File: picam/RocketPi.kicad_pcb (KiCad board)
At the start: 4 copper layers, 65 x 30 mm, 39 parts, among them J1 CAN Communication, J2 Connector_Conn_01x05_Female, J3 Conn_02x20_Counter_Clockwise_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, M1 MountingHole_2.7mm, M2 MountingHole_2.7mm, M3 MountingHole_2.7mm, M4 MountingHole_2.7mm, Q1 BSS138, Q2 AOD417, Q3 BSS138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

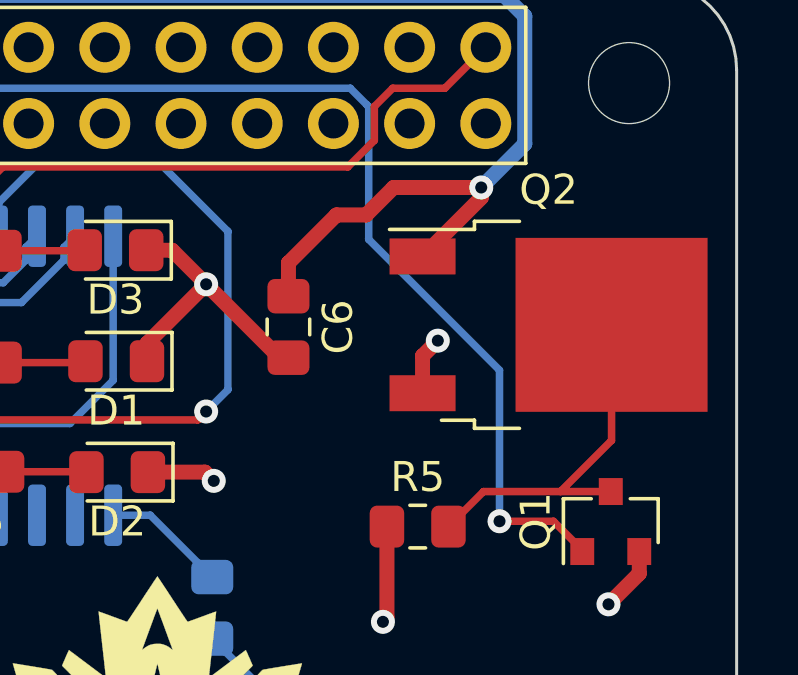
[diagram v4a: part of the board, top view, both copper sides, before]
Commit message: Fix AOD417 wiring
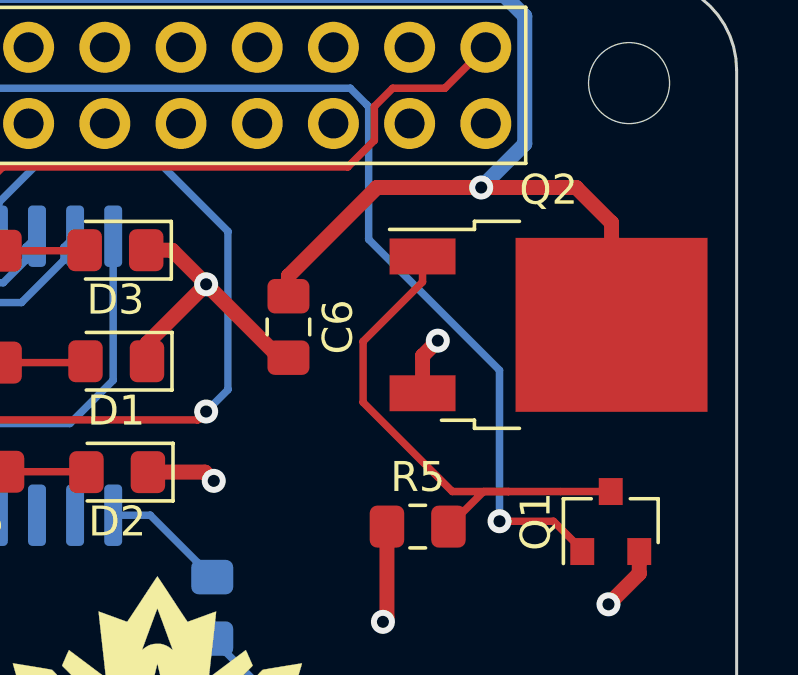
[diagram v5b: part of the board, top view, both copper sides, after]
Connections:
- Q2 pad 1: /power_pi -> Net-(Q1-Pad3)
- Q2 pad 2: Net-(Q1-Pad3) -> /power_pi
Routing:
- net Net-(Q1-Pad3): track 12.2 -> 17.7 mm
- net /power_pi: track 71.0 -> 76.2 mm
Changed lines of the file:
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@@
     (thickness 1.6)
     (drawings 21)
-    (tracks 363)
+    (tracks 368)
     (zones 0)
     (modules 39)
@@
     (pad "" smd rect (at 3.775 1.525) (size 3.05 2.75) (layers F.Paste))
     (pad 2 smd rect (at 2.1 0) (size 6.4 5.8) (layers F.Cu F.Mask)
-      (net 45 "Net-(Q1-Pad3)"))
+      (net 7 /power_pi))
     (pad 3 smd rect (at -4.2 2.28) (size 2.2 1.2) (layers F.Cu F.Paste F.Mask)
       (net 3 +5V))
     (pad 1 smd rect (at -4.2 -2.28) (size 2.2 1.2) (layers F.Cu F.Paste F.Mask)
-      (net 7 /power_pi))
+      (net 45 "Net-(Q1-Pad3)"))
     (model ${KISYS3DMOD}/Package_TO_SOT_SMD.3dshapes/TO-252-2.wrl
       (at (xyz 0 0 0))
@@
   (segment (start 74.281399 43.574601) (end 74.281399 43.549201) (width 0.5) (layer B.Cu) (net 7))
   (via (at 121.539 49.0982) (size 0.8) (drill 0.4) (layers F.Cu B.Cu) (net 7))
-  (segment (start 121.539 49.0982) (end 121.539 49.4404) (width 0.5) (layer F.Cu) (net 7))
-  (segment (start 121.539 49.4404) (end 119.5832 51.3962) (width 0.5) (layer F.Cu) (net 7))
   (segment (start 74.306799 43.574601) (end 75.184 42.6974) (width 0.5) (layer B.Cu) (net 7))
   (segment (start 74.281399 43.574601) (end 74.306799 43.574601) (width 0.5) (layer B.Cu) (net 7))
@@
   (segment (start 77.6986 42.6974) (end 122.301 42.6974) (width 0.5) (layer B.Cu) (net 7))
   (segment (start 122.301 42.6974) (end 122.991401 43.387801) (width 0.5) (layer B.Cu) (net 7))
-  (segment (start 118.618 49.0982) (end 121.539 49.0982) (width 0.5) (layer F.Cu) (net 7))
-  (segment (start 117.7036 50.0126) (end 118.618 49.0982) (width 0.5) (layer F.Cu) (net 7))
-  (segment (start 117.7036 50.0126) (end 116.713 50.0126) (width 0.5) (layer F.Cu) (net 7))
-  (segment (start 115.1128 51.6128) (end 115.1128 52.7214) (width 0.5) (layer F.Cu) (net 7))
-  (segment (start 116.713 50.0126) (end 115.1128 51.6128) (width 0.5) (layer F.Cu) (net 7))
+  (segment (start 125.8832 53.6762) (end 125.5832 53.6762) (width 0.5) (layer F.Cu) (net 7))
+  (segment (start 125.8832 50.2762) (end 125.8832 53.6762) (width 0.5) (layer F.Cu) (net 7))
+  (segment (start 124.7052 49.0982) (end 125.8832 50.2762) (width 0.5) (layer F.Cu) (net 7))
+  (segment (start 121.539 49.0982) (end 124.7052 49.0982) (width 0.5) (layer F.Cu) (net 7))
+  (segment (start 120.973315 49.0982) (end 121.539 49.0982) (width 0.5) (layer F.Cu) (net 7))
+  (segment (start 118.061 49.0982) (end 120.973315 49.0982) (width 0.5) (layer F.Cu) (net 7))
+  (segment (start 115.1128 52.0464) (end 118.061 49.0982) (width 0.5) (layer F.Cu) (net 7))
+  (segment (start 115.1128 52.7214) (end 115.1128 52.0464) (width 0.5) (layer F.Cu) (net 7))
   (segment (start 73.4314 52.4166) (end 73.406 52.442) (width 0.25) (layer F.Cu) (net 8))
   (segment (start 79.3142 50.7298) (end 79.2948 50.7492) (width 0.25) (layer F.Cu) (net 8))
@@
   (segment (start 120.4468 60.4012) (end 121.6152 59.2328) (width 0.25) (layer F.Cu) (net 45))
   (segment (start 124.1806 59.2328) (end 125.857 59.2328) (width 0.25) (layer F.Cu) (net 45))
-  (segment (start 121.6152 59.2328) (end 124.1806 59.2328) (width 0.25) (layer F.Cu) (net 45))
-  (segment (start 125.8832 57.5302) (end 125.8832 53.6762) (width 0.25) (layer F.Cu) (net 45))
-  (segment (start 124.1806 59.2328) (end 125.8832 57.5302) (width 0.25) (layer F.Cu) (net 45))
+  (segment (start 119.5832 52.2462) (end 117.602 54.2274) (width 0.25) (layer F.Cu) (net 45))
+  (segment (start 119.5832 51.3962) (end 119.5832 52.2462) (width 0.25) (layer F.Cu) (net 45))
+  (segment (start 120.574798 59.2328) (end 122.4534 59.2328) (width 0.25) (layer F.Cu) (net 45))
+  (segment (start 117.602 56.260002) (end 120.574798 59.2328) (width 0.25) (layer F.Cu) (net 45))
+  (segment (start 117.602 54.2274) (end 117.602 56.260002) (width 0.25) (layer F.Cu) (net 45))
+  (segment (start 121.6152 59.2328) (end 122.4534 59.2328) (width 0.25) (layer F.Cu) (net 45))
+  (segment (start 122.4534 59.2328) (end 124.1806 59.2328) (width 0.25) (layer F.Cu) (net 45))
   (segment (start 94.916431 48.139601) (end 99.612199 48.139601) (width 0.25) (layer B.Cu) (net 46))
   (segment (start 93.13151 49.924522) (end 94.916431 48.139601) (width 0.25) (layer B.Cu) (net 46))

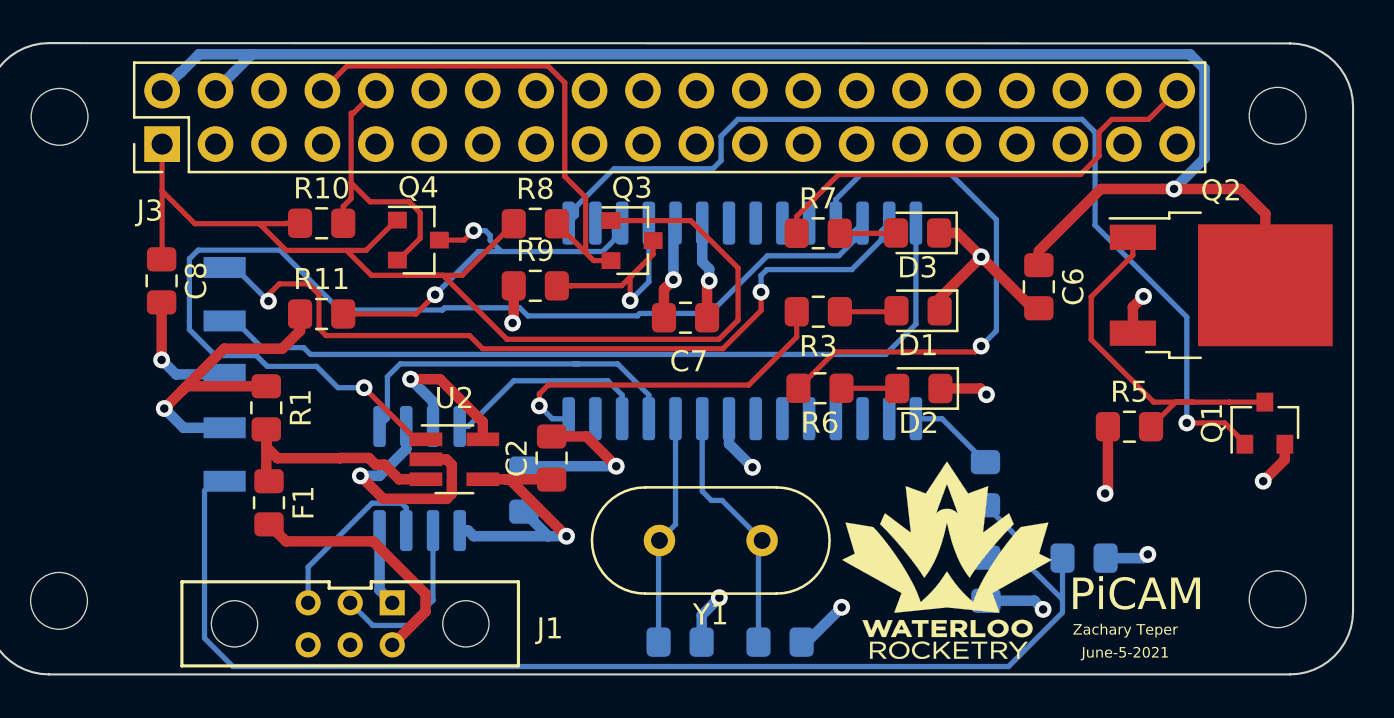
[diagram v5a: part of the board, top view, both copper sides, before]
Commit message: Rotate CAN connector 180 degrees
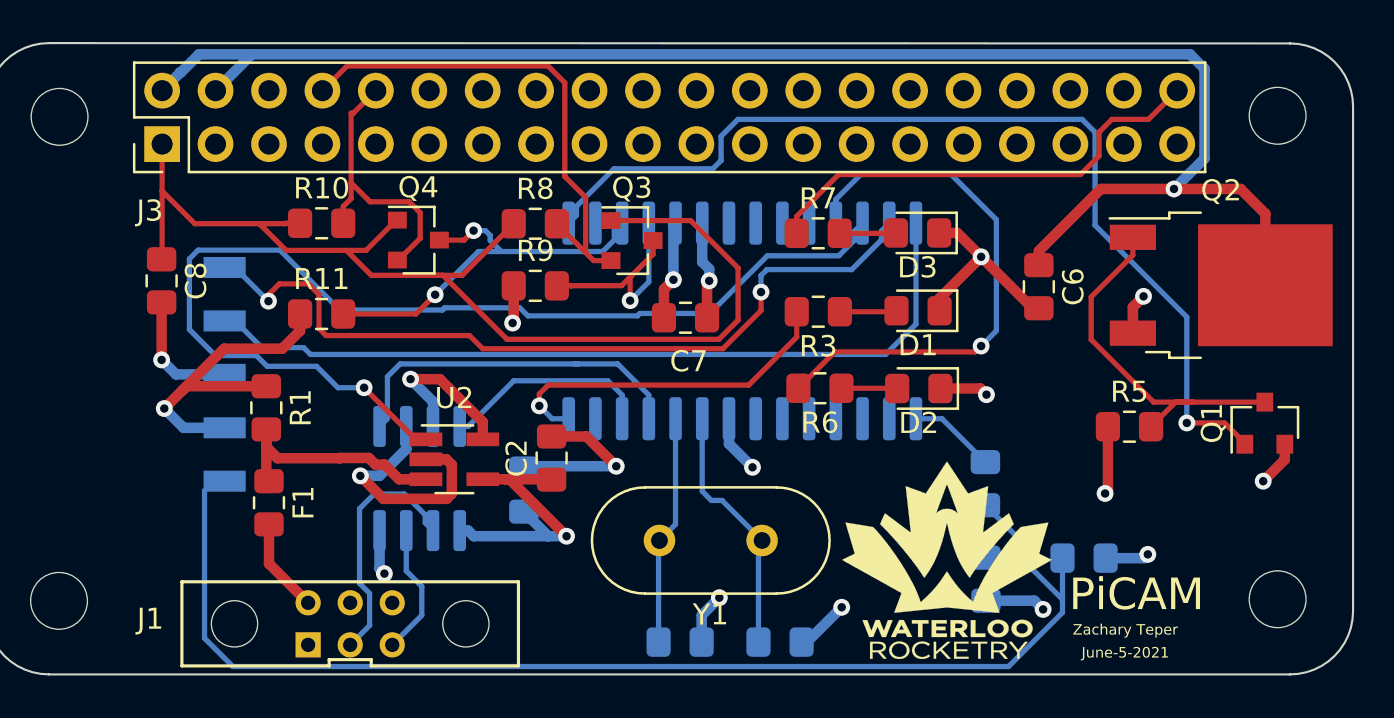
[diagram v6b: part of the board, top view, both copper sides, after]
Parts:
- turned J1 to 0 degrees
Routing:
- net Net-(F1-Pad2): track 11.9 -> 4.50 mm
- net /CANL: track 8.19 -> 11.8 mm
- net /CANH: track 8.79 -> 6.32 mm
- net GND: track 57.9 -> 56.4 mm, vias 11 -> 12

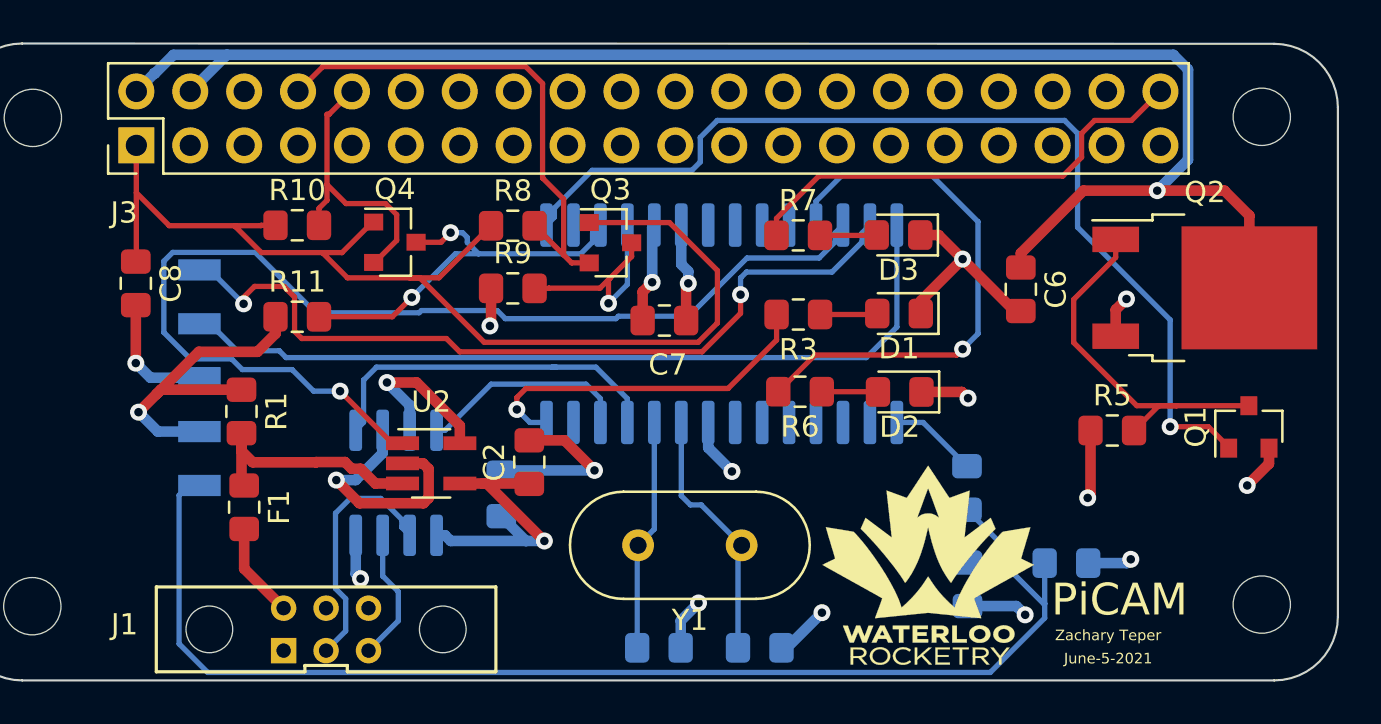
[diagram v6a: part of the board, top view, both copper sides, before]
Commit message: Add gate resistor and redo some routing
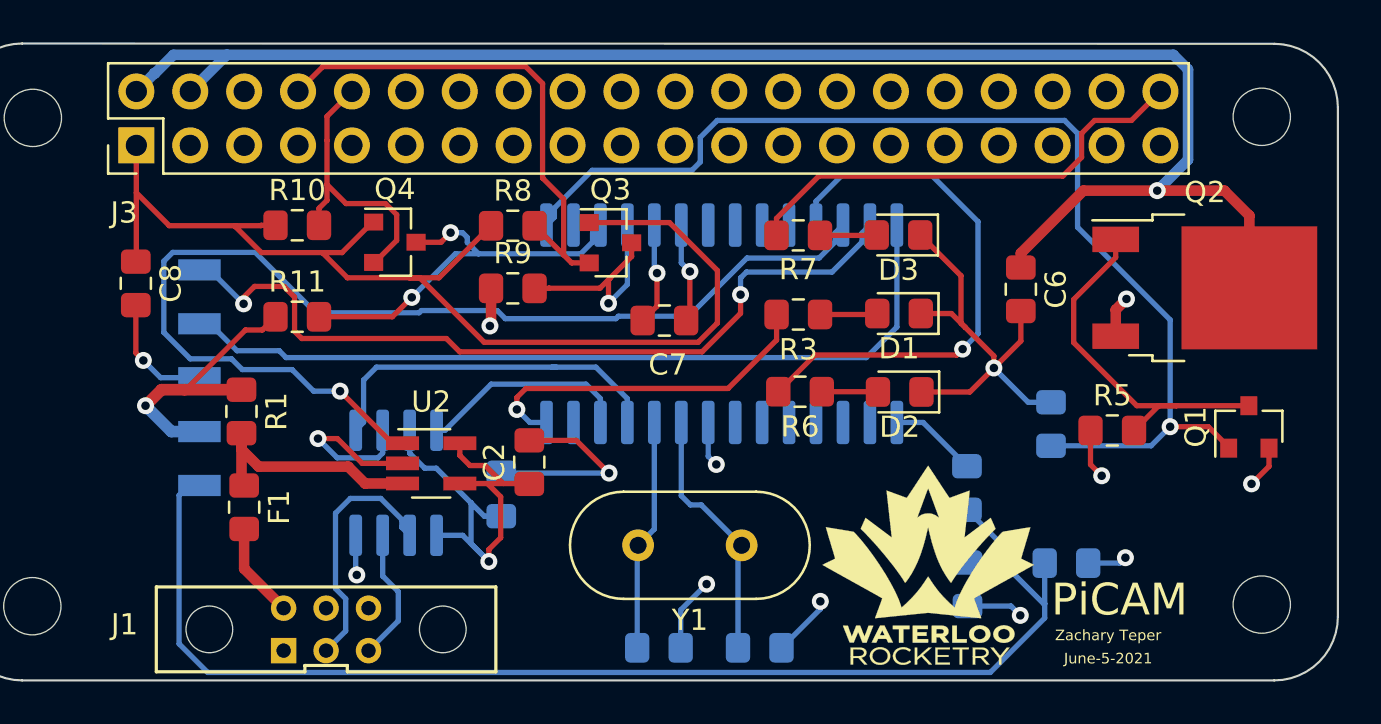
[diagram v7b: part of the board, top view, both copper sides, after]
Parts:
- added R12: 50K, Resistor_SMD:R_0805_2012Metric_Pad1.15x1.40mm_HandSolder, B.Cu at (116.5, 60.1)
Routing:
- net GND: track 56.4 -> 64.0 mm, vias 12 -> 11
- net /pi_switching: track 47.1 -> 53.1 mm
- net +5V: track 52.6 -> 50.4 mm, vias 8 -> 7

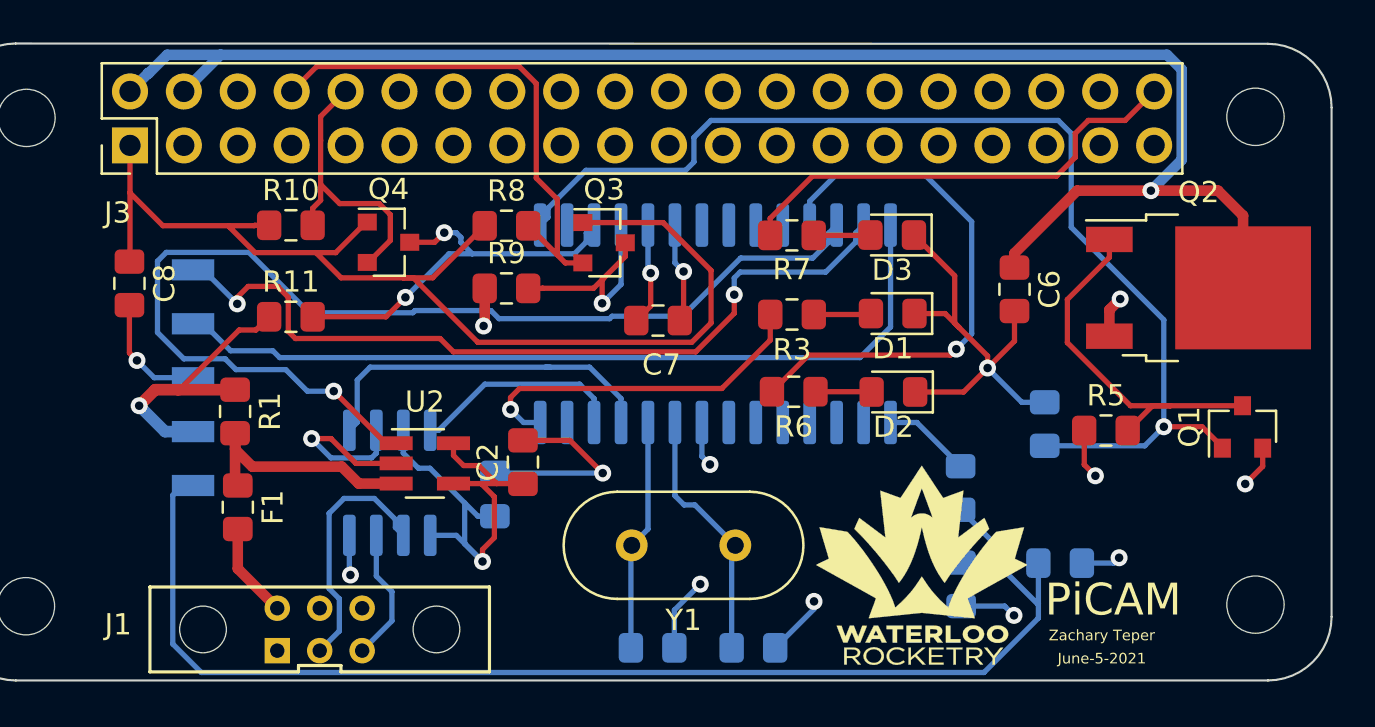
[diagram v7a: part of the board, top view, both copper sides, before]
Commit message: Fix routing and implement Lana's comments
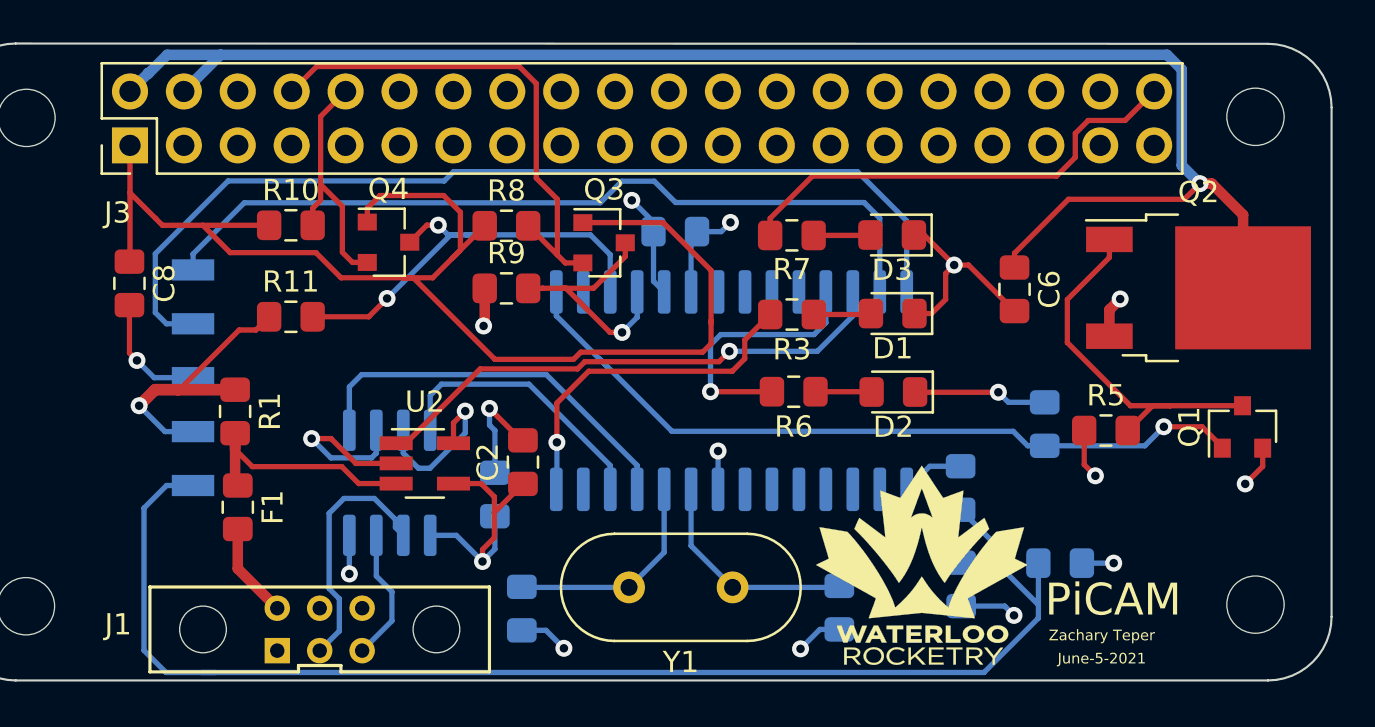
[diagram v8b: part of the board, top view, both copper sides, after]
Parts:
- C7: moved to B.Cu
- moved C5 6.43 mm to (91.9, 68.8), turned to 270 degrees
- moved C4 4.47 mm to (106.9, 68.7), turned to 270 degrees
- moved C7 4.27 mm to (99.1, 51.0)
- moved U3 3.24 mm to (101.8, 58.5)
- moved Y1 1.99 mm to (101.8, 67.8)
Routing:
- net /CURRENT_SENSE: track 52.4 -> 25.1 mm
- net /pi_switching: track 53.1 -> 36.4 mm
- net Net-(R6-Pad2): track 26.0 -> 12.4 mm
- net GND: track 64.0 -> 53.1 mm, vias 11 -> 12
- net /ICSPDAT: track 38.9 -> 46.6 mm
- net +3V3: track 55.4 -> 62.9 mm
- net /~MCLR: track 61.3 -> 65.0 mm
- net /CAN_RX: track 10.0 -> 13.1 mm
- net +5V: track 50.4 -> 47.6 mm, vias 7 -> 8
- net /PIC_TX: track 19.0 -> 20.9 mm
- net /OSC1: track 12.2 -> 10.5 mm
- net /Pi_Rx: track 13.5 -> 11.9 mm
- net /CAN_TX: track 17.1 -> 18.7 mm
- net Net-(R4-Pad1): track 4.16 -> 2.99 mm
- net /PIC_RX: track 11.1 -> 11.8 mm
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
